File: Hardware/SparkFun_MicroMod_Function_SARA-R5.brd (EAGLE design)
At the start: 37.5 x 65 mm, 121 parts, among them J1 MICROMOD_FUNCTION_STANDARD, J2 U.FL, J4 U.FL, J9 NANO_SIM, Q2 310mA/60V/1.6Ω, Q3 310mA/60V/1.6Ω, Q5 310mA/60V/1.6Ω, Q6 310mA/60V/1.6Ω, U1 SARA-R510M8S, U11 74HC1G04, U2 SN74AVC4T774PW, U3 3.3V, U4 EEPROM, U5 AP7361C-33FGE

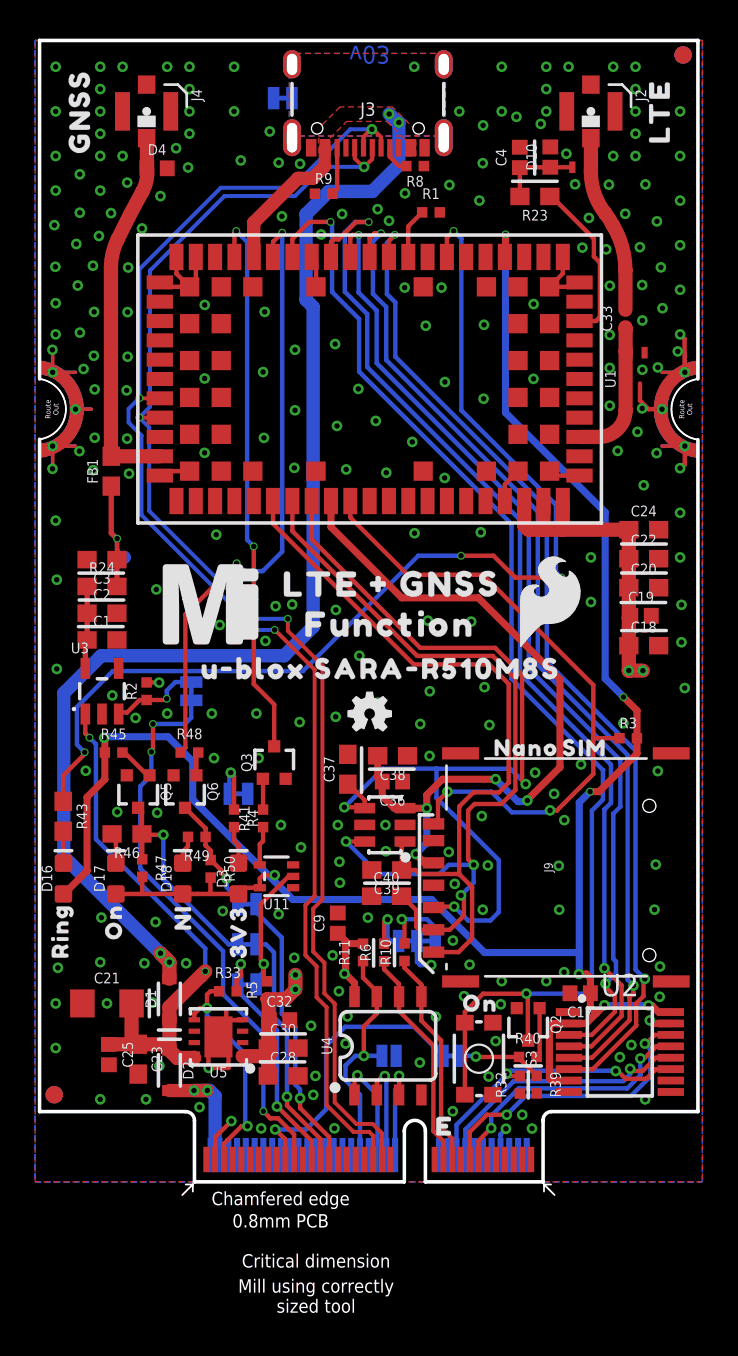
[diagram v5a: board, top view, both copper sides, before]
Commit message: ESD diode position and removed L1
-Moved ESD diode D10 to the other side of L2, to put it directly next to the u.fl connector
-removed L1 (it was previously DNP)
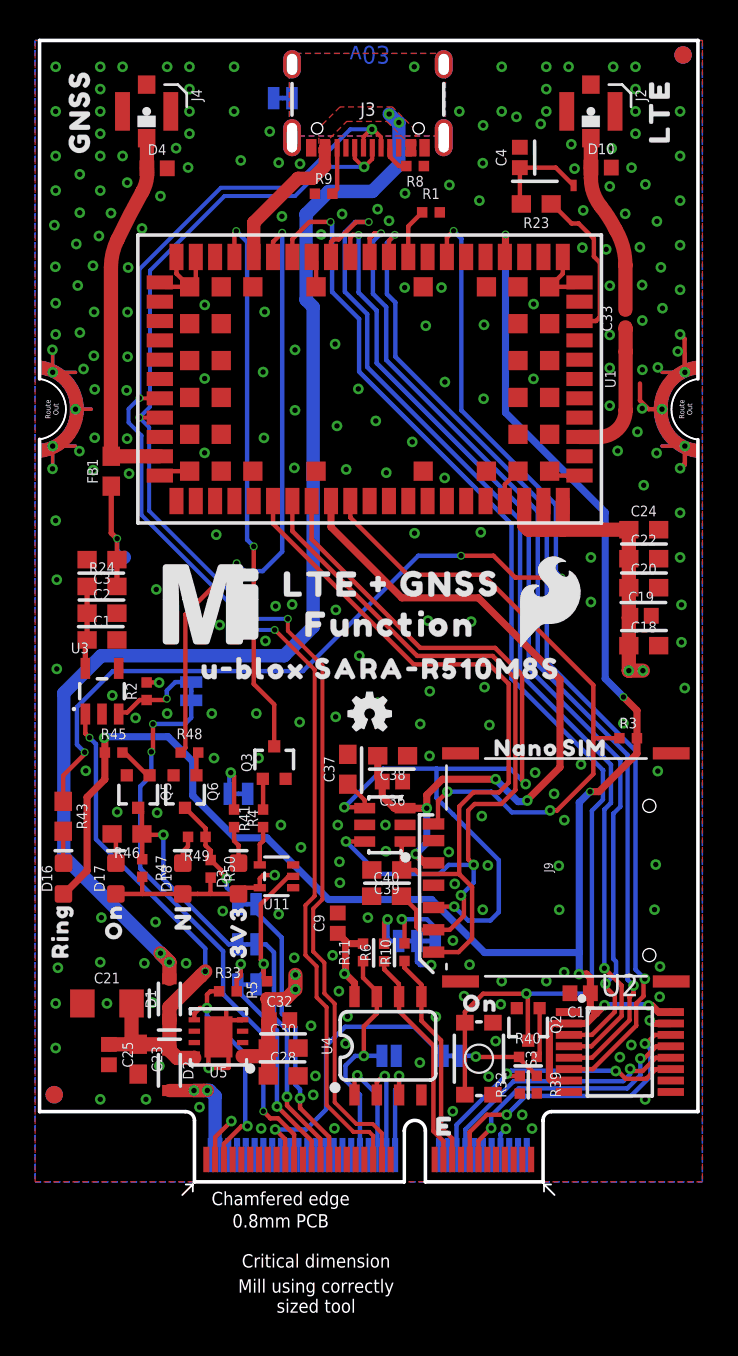
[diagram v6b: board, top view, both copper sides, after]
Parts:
- removed L1: DNP, New_Parts:0402_COILCRAFT
- moved D10 2.96 mm to (32.2, 57.8), turned to 0 degrees
- moved L2 1.04 mm to (31.1, 56.7)
- moved R23 0.43 mm to (28.5, 55.7)
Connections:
- net GND: no longer L1.P$2
- net LTE_ANT: no longer L1.P$1
- net N$11: now also D10.1
- net N$18: no longer D10.1
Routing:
- net N$18: track 4.64 -> 5.62 mm
- net N$11: track 10.4 -> 11.3 mm

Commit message: acid traps and measures
-fixed some acid traps and routed some GNDs off of pads
-measures to everything
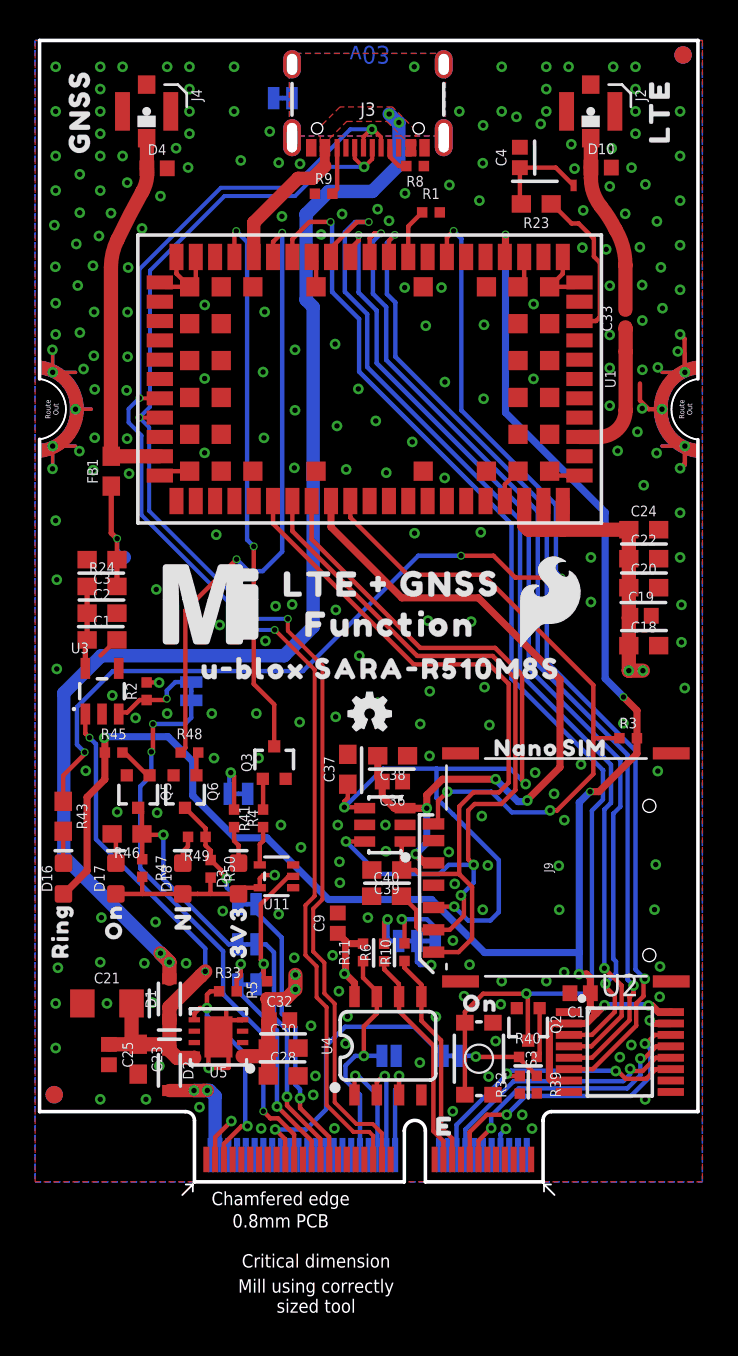
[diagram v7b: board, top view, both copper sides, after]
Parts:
- R3: value 1k -> 100k
- moved LOGO3 16.8 mm to (50.7, 74.4)
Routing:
- net GND: track 36.0 -> 39.2 mm
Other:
- board text added: "Measurement Units: MM"

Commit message: USB lines updated for correct impedance calcs
-updated trace width and spacing to hit a 90 ohm differential impedance on D+/D-
-updated calculation text paragraph in SCH
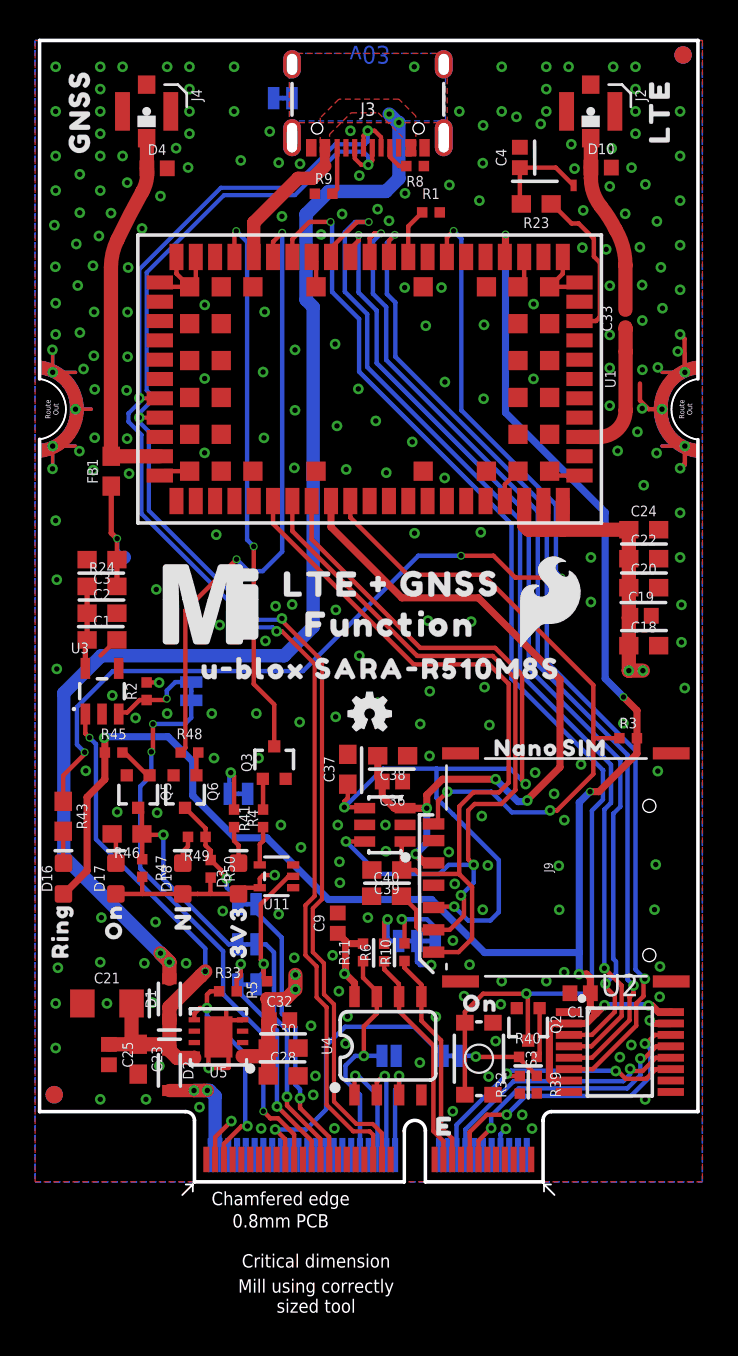
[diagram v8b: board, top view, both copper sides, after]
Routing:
- net USB_P: track 77.0 -> 78.3 mm
- net GND: vias 249 -> 251
